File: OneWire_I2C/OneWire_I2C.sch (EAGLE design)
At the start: 12 parts, among them Q1 TP0602N3

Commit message: Added Schematic and board for DS2482-800
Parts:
- removed J2: (no value), con-amp-mt:L03P
- added J3: (no value), SparkFun-Connectors:M03SCREW
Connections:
- net 1WR: now also J3.2; no longer J2-2.S
- net GND: now also J3.3; no longer J2-1.S
- net VCC: now also J3.1; no longer J2-3.S
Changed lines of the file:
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@@
 <classes>
 <class number="0" name="default" width="0" drill="0">
+<clearance class="0" value="0.205"/>
 </class>
 </classes>
 <parts>
-<part name="J2" library="con-amp-mt" deviceset="L03P" device=""/>
 <part name="SUPPLY3" library="supply2" deviceset="GND" device=""/>
 <part name="SUPPLY4" library="supply2" deviceset="GND" device=""/>
@@
 <part name="J1" library="SparkFun-Connectors" deviceset="M05" device="PTH"/>
 <part name="FRAME1" library="frames" deviceset="LETTER_L" device=""/>
+<part name="J3" library="SparkFun-Connectors" deviceset="M03" device="SCREW"/>
 </parts>
 <sheets>
@@
 </plain>
 <instances>
-<instance part="J2" gate="-1" x="127" y="60.96" rot="R180"/>
-<instance part="J2" gate="-2" x="127" y="66.04" rot="R180"/>
-<instance part="J2" gate="-3" x="127" y="71.12" rot="R180"/>
 <instance part="SUPPLY3" gate="GND" x="119.38" y="53.34"/>
 <instance part="SUPPLY4" gate="GND" x="30.48" y="53.34"/>
@@
 <instance part="FRAME1" gate="G$1" x="-45.72" y="-40.64"/>
 <instance part="FRAME1" gate="G$2" x="101.6" y="-40.64"/>
+<instance part="J3" gate="J$1" x="129.54" y="66.04" rot="R180"/>
 </instances>
 <busses>
@@
 <pinref part="R3" gate="G$1" pin="2"/>
 <wire x1="93.98" y1="81.28" x2="106.68" y2="81.28" width="0.1524" layer="91"/>
-<pinref part="J2" gate="-3" pin="S"/>
-<wire x1="121.92" y1="71.12" x2="119.38" y2="71.12" width="0.1524" layer="91"/>
-<wire x1="119.38" y1="71.12" x2="119.38" y2="81.28" width="0.1524" layer="91"/>
 <wire x1="119.38" y1="81.28" x2="106.68" y2="81.28" width="0.1524" layer="91"/>
 <junction x="93.98" y="81.28"/>
 <junction x="106.68" y="81.28"/>
+<pinref part="J3" gate="J$1" pin="1"/>
+<wire x1="119.38" y1="81.28" x2="119.38" y2="68.58" width="0.1524" layer="91"/>
+<wire x1="119.38" y1="68.58" x2="121.92" y2="68.58" width="0.1524" layer="91"/>
 </segment>
 <segment>
@@
 </segment>
 <segment>
-<pinref part="SUPPLY3" gate="GND" pin="GND"/>
-<pinref part="J2" gate="-1" pin="S"/>
-<wire x1="119.38" y1="55.88" x2="119.38" y2="60.96" width="0.1524" layer="91"/>
-<wire x1="119.38" y1="60.96" x2="121.92" y2="60.96" width="0.1524" layer="91"/>
-</segment>
-<segment>
 <pinref part="C1" gate="G$1" pin="2"/>
 <pinref part="GND" gate="GND" pin="GND"/>
@@
 <wire x1="30.48" y1="55.88" x2="30.48" y2="60.96" width="0.1524" layer="91"/>
 <wire x1="30.48" y1="60.96" x2="25.4" y2="60.96" width="0.1524" layer="91"/>
+</segment>
+<segment>
+<pinref part="J3" gate="J$1" pin="3"/>
+<pinref part="SUPPLY3" gate="GND" pin="GND"/>
+<wire x1="121.92" y1="63.5" x2="119.38" y2="63.5" width="0.1524" layer="91"/>
+<wire x1="119.38" y1="63.5" x2="119.38" y2="55.88" width="0.1524" layer="91"/>
 </segment>
 </net>
@@
 <pinref part="J1" gate="G$1" pin="2"/>
 <wire x1="53.34" y1="68.58" x2="25.4" y2="68.58" width="0.1524" layer="91"/>
+<junction x="53.34" y="68.58"/>
 </segment>
 </net>
@@
 <pinref part="J1" gate="G$1" pin="3"/>
 <wire x1="55.88" y1="66.04" x2="25.4" y2="66.04" width="0.1524" layer="91"/>
+<junction x="55.88" y="66.04"/>
 </segment>
 </net>
@@
 </segment>
 <segment>
-<pinref part="J2" gate="-2" pin="S"/>
 <pinref part="W1" gate="G$1" pin="IO"/>
-<wire x1="121.92" y1="66.04" x2="111.76" y2="66.04" width="0.1524" layer="91"/>
 <pinref part="Q1" gate="G$1" pin="D"/>
 <wire x1="111.76" y1="66.04" x2="101.6" y2="66.04" width="0.1524" layer="91"/>
@@
 <wire x1="111.76" y1="66.04" x2="111.76" y2="60.96" width="0.1524" layer="91"/>
 <label x="111.76" y="60.96" size="1.778" layer="95" rot="R270" xref="yes"/>
-</segment>
-</net>
+<pinref part="J3" gate="J$1" pin="2"/>
+<wire x1="111.76" y1="66.04" x2="121.92" y2="66.04" width="0.1524" layer="91"/>
+</segment>
+</net>

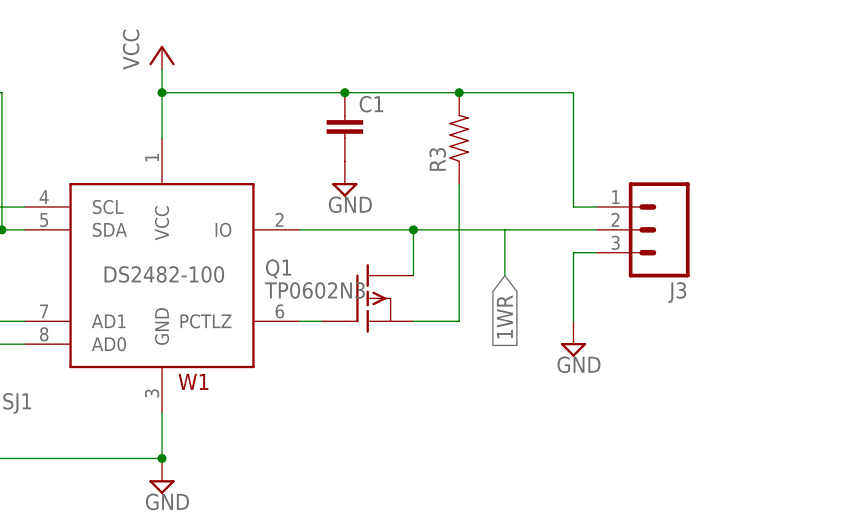
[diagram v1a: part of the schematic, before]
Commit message: Tweaks to I2C 1Wire bridge boards
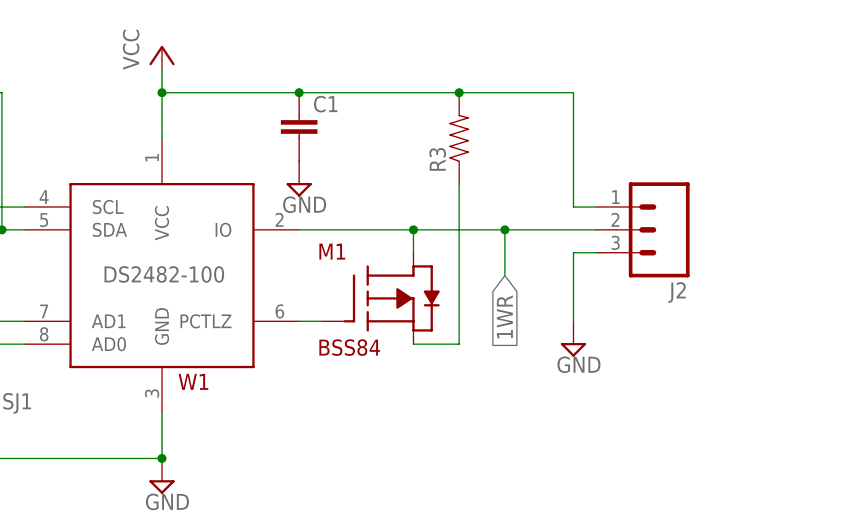
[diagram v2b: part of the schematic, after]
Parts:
- removed Q1: TP0602N3, transistor-fet:TP0602N3
- added M1: BSS84, Puffin:BSS84
- renumbered J3 to J2
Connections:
- removed net PCTL: Q1.G, W1.PCTLZ
- new net N$1: M1.1, W1.PCTLZ
- net 1WR: now also M1.3; no longer Q1.D
- net N$10: now also M1.2; no longer Q1.S
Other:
- moved on the sheet: C1
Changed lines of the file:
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@@
 <part name="SJ1" library="jumper" deviceset="SJ2W" device=""/>
 <part name="P+4" library="supply1" deviceset="VCC" device=""/>
-<part name="Q1" library="transistor-fet" deviceset="TP0602N3" device=""/>
 <part name="R3" library="SparkFun-Resistors" deviceset="RESISTOR" device="PTH-1/4W"/>
 <part name="J1" library="SparkFun-Connectors" deviceset="M05" device="PTH"/>
 <part name="FRAME1" library="frames" deviceset="LETTER_L" device=""/>
-<part name="J3" library="SparkFun-Connectors" deviceset="M03" device="SCREW"/>
+<part name="J2" library="SparkFun-Connectors" deviceset="M03" device="SCREW"/>
+<part name="M1" library="Puffin" deviceset="BSS84" device=""/>
 </parts>
 <sheets>
@@
 <instance part="SJ4" gate="1" x="48.26" y="81.28" rot="R180"/>
 <instance part="P+3" gate="VCC" x="30.48" y="86.36"/>
-<instance part="C1" gate="G$1" x="93.98" y="76.2"/>
+<instance part="C1" gate="G$1" x="88.9" y="76.2"/>
 <instance part="R1" gate="G$1" x="38.1" y="81.28"/>
 <instance part="R2" gate="G$1" x="38.1" y="76.2"/>
 <instance part="W1" gate="G$1" x="73.66" y="60.96"/>
 <instance part="SUPPLY1" gate="GND" x="73.66" y="38.1"/>
-<instance part="GND" gate="GND" x="93.98" y="71.12"/>
+<instance part="GND" gate="GND" x="88.9" y="71.12"/>
 <instance part="SJ2" gate="G$1" x="40.64" y="45.72" rot="MR0"/>
 <instance part="SJ1" gate="G$1" x="53.34" y="45.72"/>
 <instance part="P+4" gate="VCC" x="40.64" y="55.88"/>
-<instance part="Q1" gate="G$1" x="96.52" y="58.42"/>
 <instance part="R3" gate="G$1" x="106.68" y="76.2" rot="R90"/>
 <instance part="J1" gate="G$1" x="17.78" y="66.04" rot="MR180"/>
 <instance part="FRAME1" gate="G$1" x="-45.72" y="-40.64"/>
 <instance part="FRAME1" gate="G$2" x="101.6" y="-40.64"/>
-<instance part="J3" gate="J$1" x="129.54" y="66.04" rot="R180"/>
+<instance part="J2" gate="J$1" x="129.54" y="66.04" rot="R180"/>
+<instance part="M1" gate="G$1" x="99.06" y="55.88"/>
 </instances>
 <busses>
@@
 <pinref part="C1" gate="G$1" pin="1"/>
 <wire x1="73.66" y1="81.28" x2="73.66" y2="76.2" width="0.1524" layer="91"/>
-<wire x1="93.98" y1="81.28" x2="73.66" y2="81.28" width="0.1524" layer="91"/>
+<wire x1="88.9" y1="81.28" x2="73.66" y2="81.28" width="0.1524" layer="91"/>
 <junction x="73.66" y="81.28"/>
 <pinref part="R3" gate="G$1" pin="2"/>
-<wire x1="93.98" y1="81.28" x2="106.68" y2="81.28" width="0.1524" layer="91"/>
+<wire x1="88.9" y1="81.28" x2="106.68" y2="81.28" width="0.1524" layer="91"/>
 <wire x1="119.38" y1="81.28" x2="106.68" y2="81.28" width="0.1524" layer="91"/>
-<junction x="93.98" y="81.28"/>
+<junction x="88.9" y="81.28"/>
 <junction x="106.68" y="81.28"/>
-<pinref part="J3" gate="J$1" pin="1"/>
+<pinref part="J2" gate="J$1" pin="1"/>
 <wire x1="119.38" y1="81.28" x2="119.38" y2="68.58" width="0.1524" layer="91"/>
 <wire x1="119.38" y1="68.58" x2="121.92" y2="68.58" width="0.1524" layer="91"/>
@@
 </segment>
 <segment>
-<pinref part="J3" gate="J$1" pin="3"/>
+<pinref part="J2" gate="J$1" pin="3"/>
 <pinref part="SUPPLY3" gate="GND" pin="GND"/>
 <wire x1="121.92" y1="63.5" x2="119.38" y2="63.5" width="0.1524" layer="91"/>
@@
 </segment>
 </net>
-<net name="PCTL" class="0">
-<segment>
-<pinref part="W1" gate="G$1" pin="PCTLZ"/>
-<pinref part="Q1" gate="G$1" pin="G"/>
-<wire x1="88.9" y1="55.88" x2="91.44" y2="55.88" width="0.1524" layer="91"/>
-</segment>
-</net>
 <net name="N$10" class="0">
 <segment>
-<pinref part="Q1" gate="G$1" pin="S"/>
 <pinref part="R3" gate="G$1" pin="1"/>
-<wire x1="101.6" y1="55.88" x2="106.68" y2="55.88" width="0.1524" layer="91"/>
-<wire x1="106.68" y1="55.88" x2="106.68" y2="71.12" width="0.1524" layer="91"/>
+<wire x1="106.68" y1="53.34" x2="106.68" y2="71.12" width="0.1524" layer="91"/>
+<pinref part="M1" gate="G$1" pin="2"/>
+<wire x1="101.6" y1="53.34" x2="106.68" y2="53.34" width="0.1524" layer="91"/>
 </segment>
 </net>
@@
 <segment>
 <pinref part="W1" gate="G$1" pin="IO"/>
-<pinref part="Q1" gate="G$1" pin="D"/>
 <wire x1="111.76" y1="66.04" x2="101.6" y2="66.04" width="0.1524" layer="91"/>
 <wire x1="101.6" y1="66.04" x2="88.9" y2="66.04" width="0.1524" layer="91"/>
-<wire x1="101.6" y1="60.96" x2="101.6" y2="66.04" width="0.1524" layer="91"/>
-<junction x="101.6" y="66.04"/>
 <wire x1="111.76" y1="66.04" x2="111.76" y2="60.96" width="0.1524" layer="91"/>
 <label x="111.76" y="60.96" size="1.778" layer="95" rot="R270" xref="yes"/>
-<pinref part="J3" gate="J$1" pin="2"/>
+<pinref part="J2" gate="J$1" pin="2"/>
 <wire x1="111.76" y1="66.04" x2="121.92" y2="66.04" width="0.1524" layer="91"/>
+<pinref part="M1" gate="G$1" pin="3"/>
+<wire x1="101.6" y1="63.5" x2="101.6" y2="66.04" width="0.1524" layer="91"/>
+<junction x="101.6" y="66.04"/>
+<junction x="111.76" y="66.04"/>
 </segment>
 </net>
+<net name="N$1" class="0">
+<segment>
+<pinref part="W1" gate="G$1" pin="PCTLZ"/>
+<wire x1="88.9" y1="55.88" x2="91.44" y2="55.88" width="0.1524" layer="91"/>
+<pinref part="M1" gate="G$1" pin="1"/>
+</segment>
+</net>

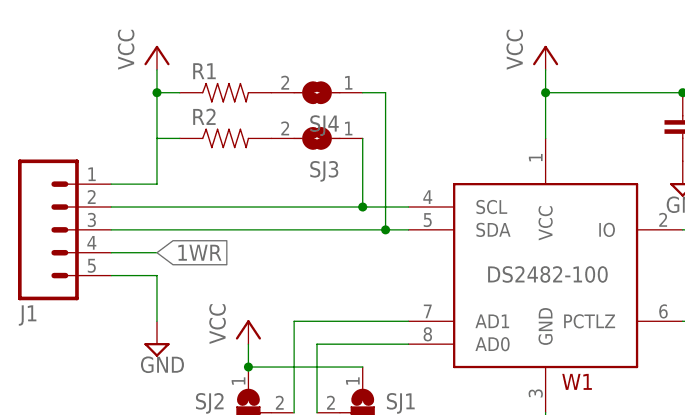
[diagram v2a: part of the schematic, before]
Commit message: Changed I2C pullup jumpers to single 3-way jumper
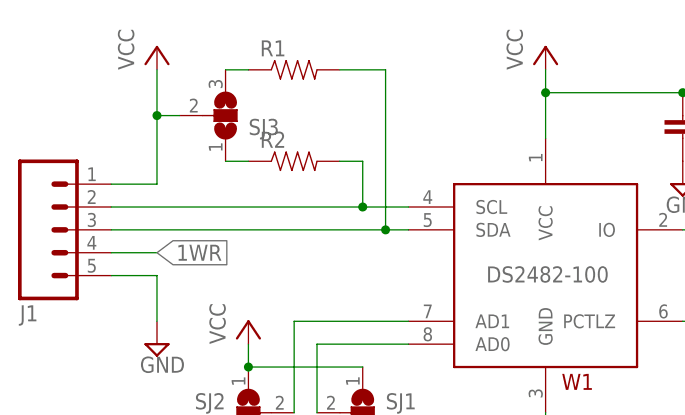
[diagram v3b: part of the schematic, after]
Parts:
- removed SJ4: (no value), jumper:SJ
- SJ3: device jumper:SJ -> jumper:SJ2W
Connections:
- removed net N$4: R1.2, SJ4.2
- new net N$2: R1.1, SJ3.3
- net N$3: now also R2.1, SJ3.1; no longer R2.2, SJ3.2
- net SCL: now also R2.2; no longer SJ3.1
- net SDA: now also R1.2; no longer SJ4.1
- net VCC: now also SJ3.2; no longer R1.1, R2.1
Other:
- moved on the sheet: R1, R2
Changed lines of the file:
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@@
 <part name="SUPPLY4" library="supply2" deviceset="GND" device=""/>
 <part name="P+1" library="supply1" deviceset="VCC" device=""/>
-<part name="SJ3" library="jumper" deviceset="SJ" device=""/>
-<part name="SJ4" library="jumper" deviceset="SJ" device=""/>
 <part name="P+3" library="supply1" deviceset="VCC" device=""/>
 <part name="C1" library="SparkFun-Capacitors" deviceset="CAP" device="0603-CAP"/>
@@
 <part name="J2" library="SparkFun-Connectors" deviceset="M03" device="SCREW"/>
 <part name="M1" library="Puffin" deviceset="BSS84" device=""/>
+<part name="SJ3" library="jumper" deviceset="SJ2W" device=""/>
 </parts>
 <sheets>
@@
 <instance part="SUPPLY4" gate="GND" x="30.48" y="53.34"/>
 <instance part="P+1" gate="VCC" x="73.66" y="86.36"/>
-<instance part="SJ3" gate="1" x="48.26" y="76.2" rot="R180"/>
-<instance part="SJ4" gate="1" x="48.26" y="81.28" rot="R180"/>
 <instance part="P+3" gate="VCC" x="30.48" y="86.36"/>
 <instance part="C1" gate="G$1" x="88.9" y="76.2"/>
-<instance part="R1" gate="G$1" x="38.1" y="81.28"/>
-<instance part="R2" gate="G$1" x="38.1" y="76.2"/>
+<instance part="R1" gate="G$1" x="45.72" y="83.82"/>
+<instance part="R2" gate="G$1" x="45.72" y="73.66"/>
 <instance part="W1" gate="G$1" x="73.66" y="60.96"/>
 <instance part="SUPPLY1" gate="GND" x="73.66" y="38.1"/>
@@
 <instance part="J2" gate="J$1" x="129.54" y="66.04" rot="R180"/>
 <instance part="M1" gate="G$1" x="99.06" y="55.88"/>
+<instance part="SJ3" gate="G$1" x="38.1" y="78.74" rot="MR180"/>
 </instances>
 <busses>
@@
 <segment>
 <pinref part="P+3" gate="VCC" pin="VCC"/>
-<wire x1="30.48" y1="83.82" x2="30.48" y2="81.28" width="0.1524" layer="91"/>
-<wire x1="30.48" y1="81.28" x2="33.02" y2="81.28" width="0.1524" layer="91"/>
-<wire x1="33.02" y1="76.2" x2="30.48" y2="76.2" width="0.1524" layer="91"/>
-<wire x1="30.48" y1="76.2" x2="30.48" y2="81.28" width="0.1524" layer="91"/>
-<junction x="30.48" y="81.28"/>
-<pinref part="R1" gate="G$1" pin="1"/>
-<pinref part="R2" gate="G$1" pin="1"/>
+<wire x1="30.48" y1="71.12" x2="30.48" y2="78.74" width="0.1524" layer="91"/>
 <pinref part="J1" gate="G$1" pin="1"/>
+<wire x1="30.48" y1="78.74" x2="30.48" y2="83.82" width="0.1524" layer="91"/>
 <wire x1="25.4" y1="71.12" x2="30.48" y2="71.12" width="0.1524" layer="91"/>
-<wire x1="30.48" y1="71.12" x2="30.48" y2="76.2" width="0.1524" layer="91"/>
+<pinref part="SJ3" gate="G$1" pin="2"/>
+<wire x1="33.02" y1="78.74" x2="30.48" y2="78.74" width="0.1524" layer="91"/>
+<junction x="30.48" y="78.74"/>
 </segment>
 <segment>
@@
 </segment>
 </net>
-<net name="N$3" class="0">
-<segment>
-<pinref part="SJ3" gate="1" pin="2"/>
+<net name="SCL" class="0">
+<segment>
+<pinref part="W1" gate="G$1" pin="SCL"/>
+<pinref part="J1" gate="G$1" pin="2"/>
+<wire x1="58.42" y1="68.58" x2="53.34" y2="68.58" width="0.1524" layer="91"/>
 <pinref part="R2" gate="G$1" pin="2"/>
-</segment>
-</net>
-<net name="N$4" class="0">
-<segment>
-<pinref part="SJ4" gate="1" pin="2"/>
-<pinref part="R1" gate="G$1" pin="2"/>
-</segment>
-</net>
-<net name="SCL" class="0">
-<segment>
-<pinref part="W1" gate="G$1" pin="SCL"/>
-<pinref part="SJ3" gate="1" pin="1"/>
-<wire x1="53.34" y1="68.58" x2="58.42" y2="68.58" width="0.1524" layer="91"/>
-<wire x1="53.34" y1="76.2" x2="53.34" y2="68.58" width="0.1524" layer="91"/>
-<pinref part="J1" gate="G$1" pin="2"/>
 <wire x1="53.34" y1="68.58" x2="25.4" y2="68.58" width="0.1524" layer="91"/>
+<wire x1="50.8" y1="73.66" x2="53.34" y2="73.66" width="0.1524" layer="91"/>
+<wire x1="53.34" y1="73.66" x2="53.34" y2="68.58" width="0.1524" layer="91"/>
 <junction x="53.34" y="68.58"/>
 </segment>
@@
 <segment>
 <pinref part="W1" gate="G$1" pin="SDA"/>
-<pinref part="SJ4" gate="1" pin="1"/>
-<wire x1="55.88" y1="66.04" x2="58.42" y2="66.04" width="0.1524" layer="91"/>
-<wire x1="53.34" y1="81.28" x2="55.88" y2="81.28" width="0.1524" layer="91"/>
-<wire x1="55.88" y1="81.28" x2="55.88" y2="66.04" width="0.1524" layer="91"/>
 <pinref part="J1" gate="G$1" pin="3"/>
+<wire x1="58.42" y1="66.04" x2="55.88" y2="66.04" width="0.1524" layer="91"/>
+<pinref part="R1" gate="G$1" pin="2"/>
 <wire x1="55.88" y1="66.04" x2="25.4" y2="66.04" width="0.1524" layer="91"/>
+<wire x1="50.8" y1="83.82" x2="55.88" y2="83.82" width="0.1524" layer="91"/>
+<wire x1="55.88" y1="83.82" x2="55.88" y2="66.04" width="0.1524" layer="91"/>
 <junction x="55.88" y="66.04"/>
 </segment>
@@
 </segment>
 </net>
+<net name="N$2" class="0">
+<segment>
+<pinref part="R1" gate="G$1" pin="1"/>
+<pinref part="SJ3" gate="G$1" pin="3"/>
+<wire x1="40.64" y1="83.82" x2="38.1" y2="83.82" width="0.1524" layer="91"/>
+</segment>
+</net>
+<net name="N$3" class="0">
+<segment>
+<pinref part="R2" gate="G$1" pin="1"/>
+<pinref part="SJ3" gate="G$1" pin="1"/>
+<wire x1="40.64" y1="73.66" x2="38.1" y2="73.66" width="0.1524" layer="91"/>
+</segment>
+</net>
